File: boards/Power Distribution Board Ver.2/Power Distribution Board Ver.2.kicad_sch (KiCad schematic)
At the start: 89 parts, among them J1 Screw_Terminal_01x02, J2 Screw_Terminal_01x06, J3 Screw_Terminal_01x06, J4 Screw_Terminal_01x06, K1 Relay, K2 Relay, K3 Relay, K4 Relay, K5 Relay, K6 Relay, SW1 SW_Push_Open, U1 SIC431AED-T1-GE3, U2 SIC431AED-T1-GE3, U3 SIC431AED-T1-GE3

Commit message: Edit PCB
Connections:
- net 5V_OUT_1: no longer D7.2 (K), D9.2 (K)
- net 5V_OUT_2: now also D7.2 (K)
- net 5V_OUT_3: now also D9.2 (K)
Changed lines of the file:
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@@
     (effects (font (size 1.27 1.27)) (justify left))
   )
-  (hierarchical_label "5V_OUT_1" (shape output) (at 229.87 226.06 0) (fields_autoplaced)
+  (hierarchical_label "5V_OUT_2" (shape output) (at 229.87 226.06 0) (fields_autoplaced)
     (effects (font (size 1.27 1.27)) (justify left))
   )
@@
     (effects (font (size 1.27 1.27)) (justify left))
   )
-  (hierarchical_label "5V_OUT_1" (shape output) (at 226.822 286.512 0) (fields_autoplaced)
+  (hierarchical_label "5V_OUT_3" (shape output) (at 226.822 286.512 0) (fields_autoplaced)
     (effects (font (size 1.27 1.27)) (justify left))
   )

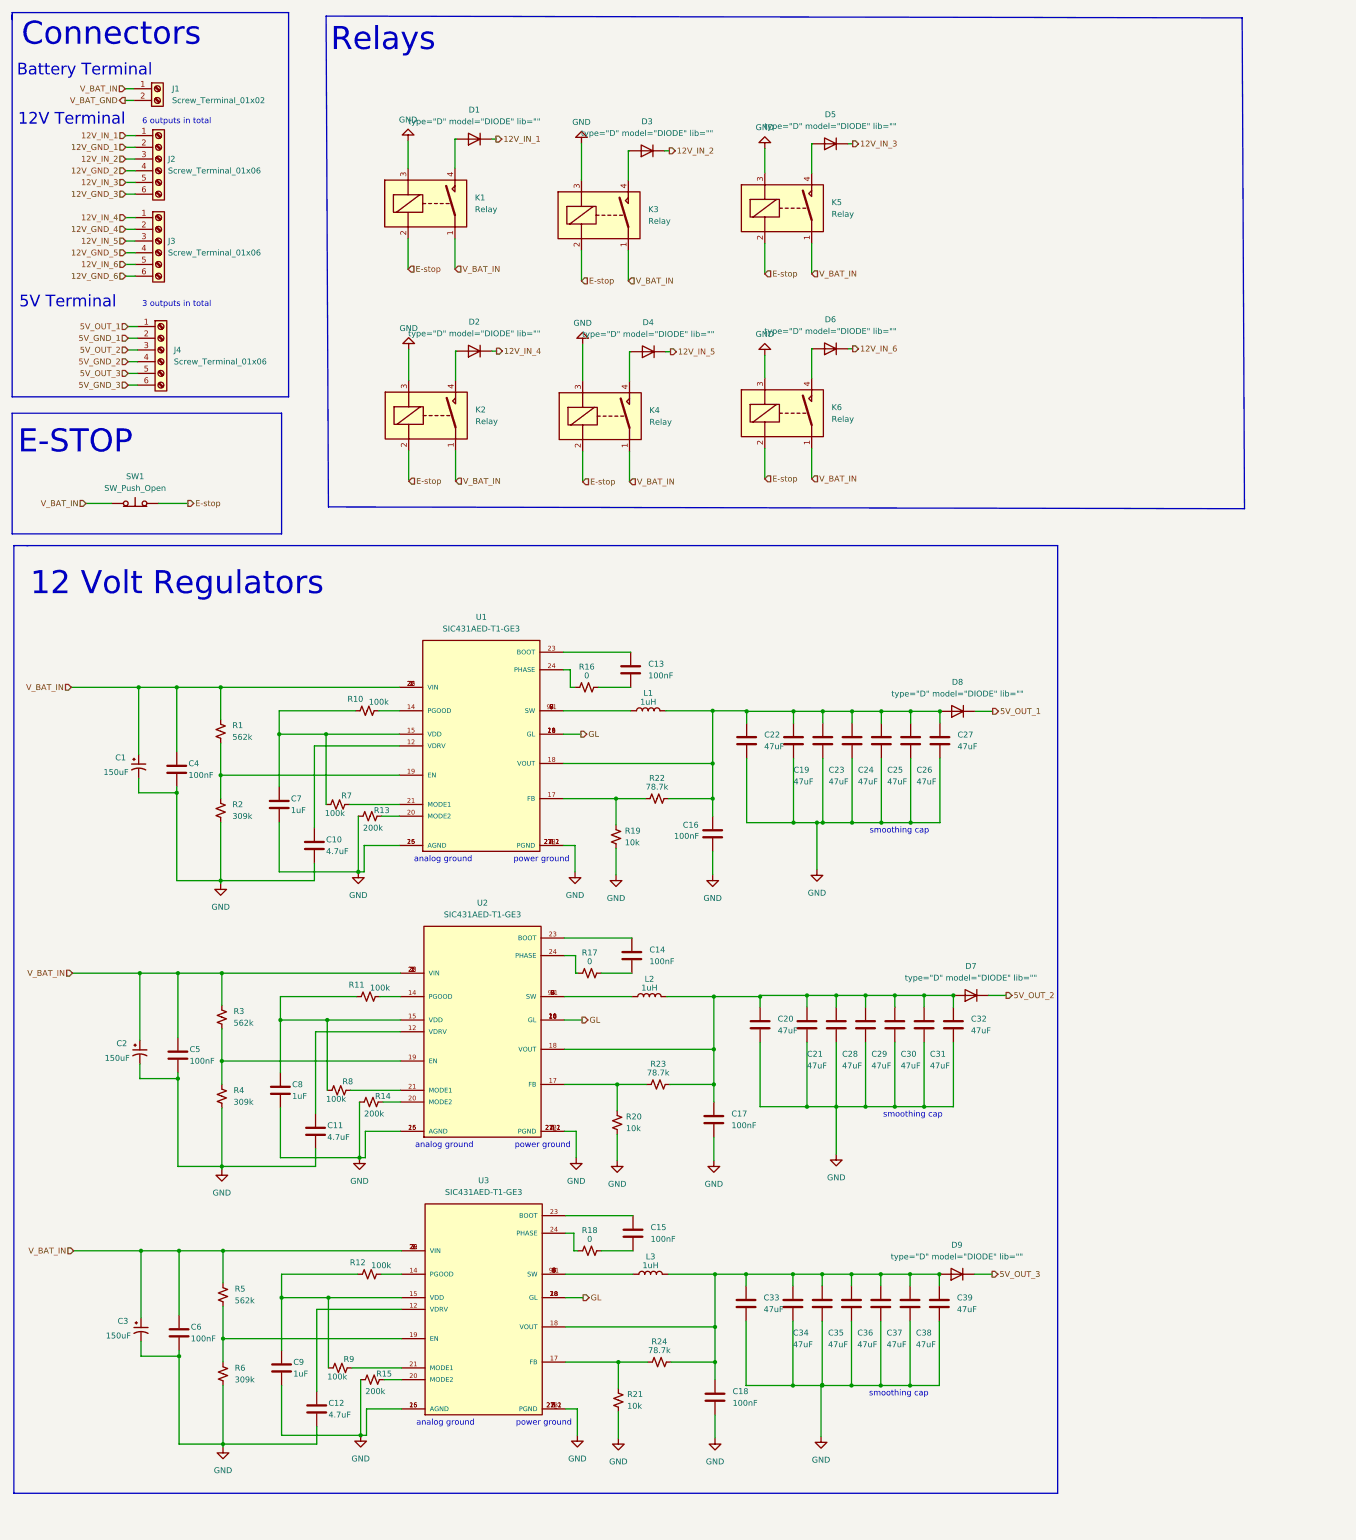
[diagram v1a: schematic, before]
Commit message: Updated GND
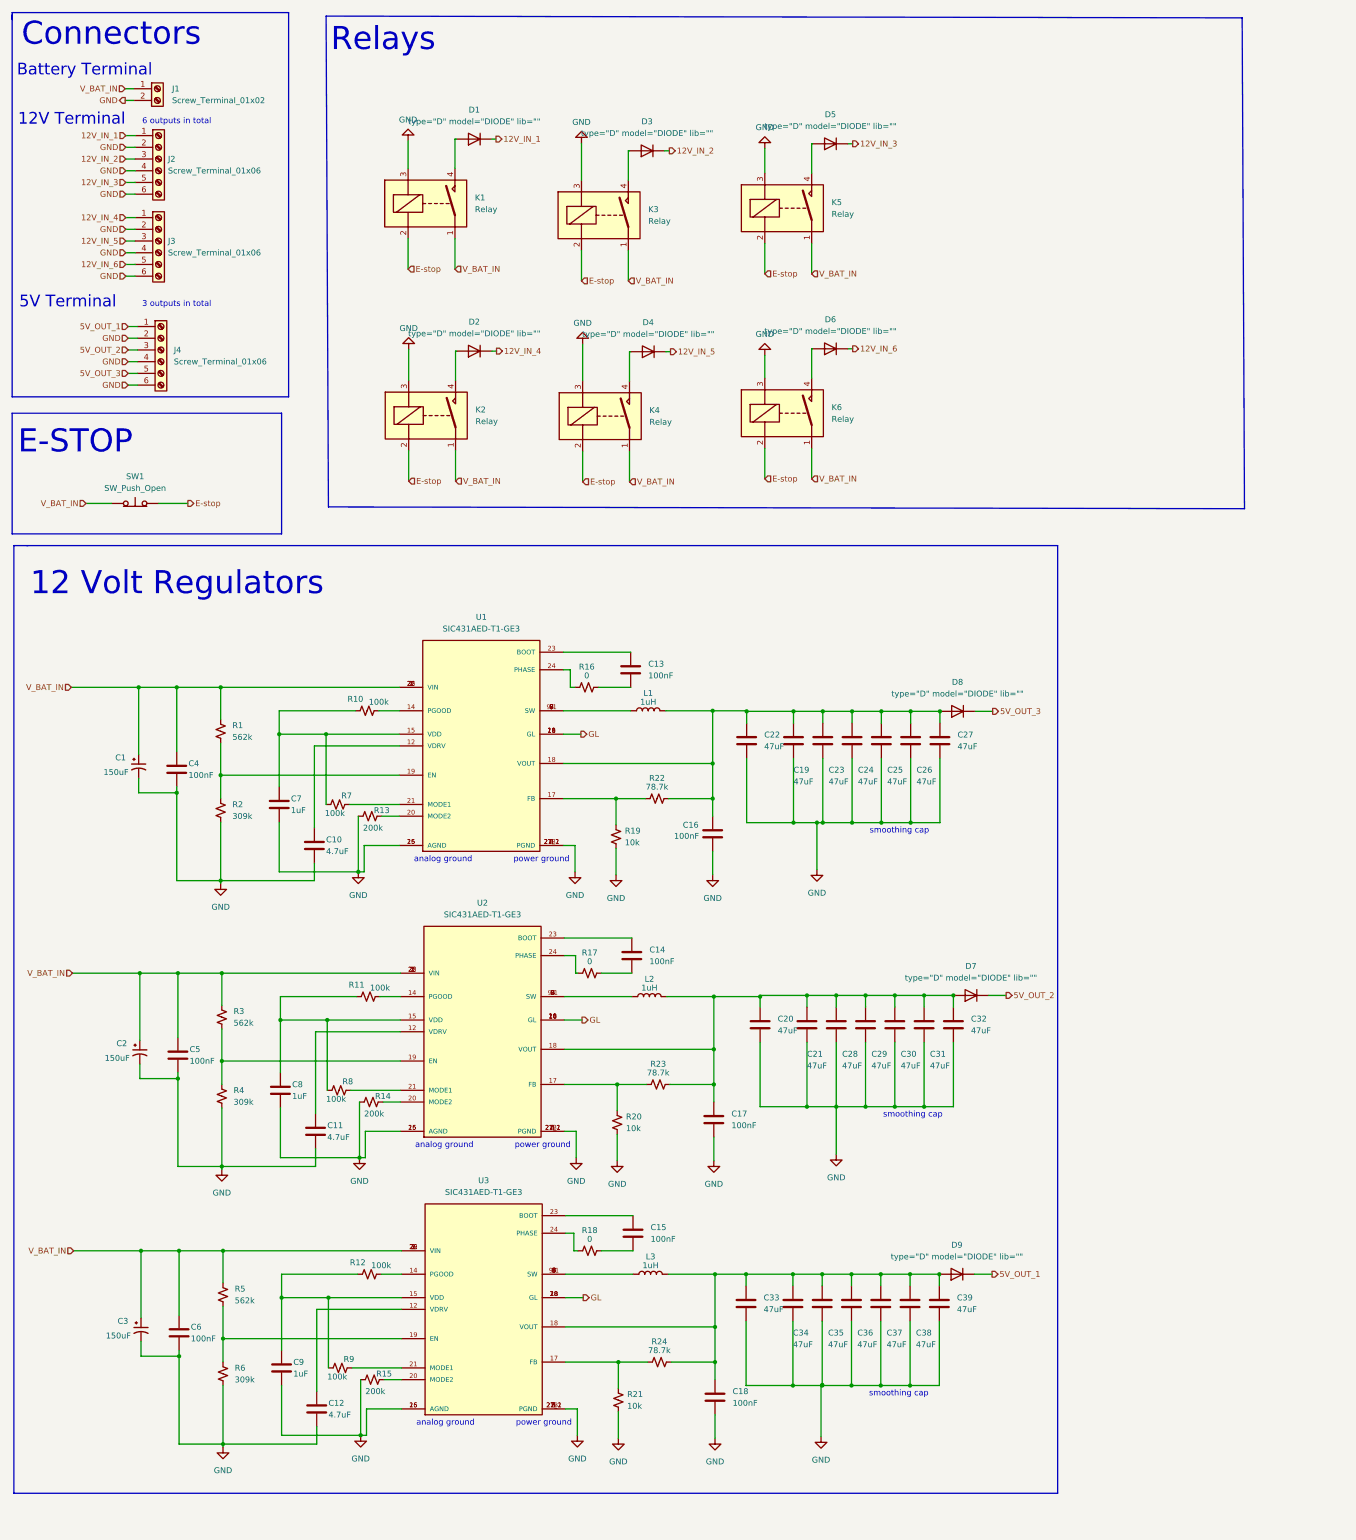
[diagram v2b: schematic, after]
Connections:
- net 12V_GND_1 is gone; now on net GND: J2.2 (Pin_2)
- net 12V_GND_2 is gone; now on net GND: J2.4 (Pin_4)
- net 12V_GND_3 is gone; now on net GND: J2.6 (Pin_6)
- net 12V_GND_4 is gone; now on net GND: J3.2 (Pin_2)
- net 12V_GND_5 is gone; now on net GND: J3.4 (Pin_4)
- net 12V_GND_6 is gone; now on net GND: J3.6 (Pin_6)
- net 5V_GND_1 is gone; now on net GND: J4.2 (Pin_2)
- net 5V_GND_2 is gone; now on net GND: J4.4 (Pin_4)
- net 5V_GND_3 is gone; now on net GND: J4.6 (Pin_6)
- net V_BAT_GND is gone; now on net GND: J1.2 (Pin_2)
- net 5V_OUT_1: now also D9.2 (K); no longer D8.2 (K)
- net 5V_OUT_3: now also D8.2 (K); no longer D9.2 (K)
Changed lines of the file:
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@@
     (effects (font (size 1.27 1.27)) (justify left))
   )
-  (hierarchical_label "5V_GND_3" (shape input) (at 39.497 93.726 180) (fields_autoplaced)
+  (hierarchical_label "GND" (shape input) (at 39.497 93.726 180) (fields_autoplaced)
     (effects (font (size 1.27 1.27)) (justify right))
   )
@@
     (effects (font (size 1.27 1.27)) (justify right))
   )
-  (hierarchical_label "12V_GND_3" (shape input) (at 38.989 52.324 180) (fields_autoplaced)
+  (hierarchical_label "GND" (shape input) (at 38.989 52.324 180) (fields_autoplaced)
     (effects (font (size 1.27 1.27)) (justify right))
   )
@@
     (effects (font (size 1.27 1.27)) (justify left))
   )
-  (hierarchical_label "12V_GND_1" (shape input) (at 38.989 42.164 180) (fields_autoplaced)
+  (hierarchical_label "GND" (shape input) (at 38.989 42.164 180) (fields_autoplaced)
     (effects (font (size 1.27 1.27)) (justify right))
   )
-  (hierarchical_label "5V_GND_2" (shape input) (at 39.497 88.646 180) (fields_autoplaced)
+  (hierarchical_label "GND" (shape input) (at 39.497 88.646 180) (fields_autoplaced)
     (effects (font (size 1.27 1.27)) (justify right))
   )
@@
     (effects (font (size 1.27 1.27)) (justify left))
   )
-  (hierarchical_label "12V_GND_5" (shape input) (at 38.989 65.024 180) (fields_autoplaced)
+  (hierarchical_label "GND" (shape input) (at 38.989 65.024 180) (fields_autoplaced)
     (effects (font (size 1.27 1.27)) (justify right))
   )
@@
     (effects (font (size 1.27 1.27)) (justify left))
   )
-  (hierarchical_label "12V_GND_2" (shape input) (at 38.989 47.244 180) (fields_autoplaced)
+  (hierarchical_label "GND" (shape input) (at 38.989 47.244 180) (fields_autoplaced)
     (effects (font (size 1.27 1.27)) (justify right))
   )
@@
     (effects (font (size 1.27 1.27)) (justify left))
   )
-  (hierarchical_label "V_BAT_GND" (shape output) (at 38.862 32.004 180) (fields_autoplaced)
+  (hierarchical_label "GND" (shape output) (at 38.862 32.004 180) (fields_autoplaced)
     (effects (font (size 1.27 1.27)) (justify right))
   )
@@
     (effects (font (size 1.27 1.27)) (justify left))
   )
-  (hierarchical_label "5V_OUT_3" (shape output) (at 226.822 286.512 0) (fields_autoplaced)
+  (hierarchical_label "5V_OUT_1" (shape output) (at 226.822 286.512 0) (fields_autoplaced)
     (effects (font (size 1.27 1.27)) (justify left))
   )
-  (hierarchical_label "5V_OUT_1" (shape output) (at 226.949 164.465 0) (fields_autoplaced)
+  (hierarchical_label "5V_OUT_3" (shape output) (at 226.949 164.465 0) (fields_autoplaced)
     (effects (font (size 1.27 1.27)) (justify left))
   )
@@
     (effects (font (size 1.27 1.27)) (justify left))
   )
-  (hierarchical_label "5V_GND_1" (shape input) (at 39.497 83.566 180) (fields_autoplaced)
+  (hierarchical_label "GND" (shape input) (at 39.497 83.566 180) (fields_autoplaced)
     (effects (font (size 1.27 1.27)) (justify right))
   )
@@
     (effects (font (size 1.27 1.27)) (justify left))
   )
-  (hierarchical_label "12V_GND_4" (shape input) (at 38.989 59.944 180) (fields_autoplaced)
+  (hierarchical_label "GND" (shape input) (at 38.989 59.944 180) (fields_autoplaced)
     (effects (font (size 1.27 1.27)) (justify right))
   )
-  (hierarchical_label "12V_GND_6" (shape input) (at 38.989 70.104 180) (fields_autoplaced)
+  (hierarchical_label "GND" (shape input) (at 38.989 70.104 180) (fields_autoplaced)
     (effects (font (size 1.27 1.27)) (justify right))
   )

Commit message: PCBPCB Circuit Design Finished
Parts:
- renumbered C20 to C19, C21 to C20, C28 to C21, C29 to C22, C30 to C23, C31 to C24, C32 to C25, C22 to C26, C19 to C27, C23 to C28, C24 to C29, C25 to C30, C26 to C31, C27 to C32

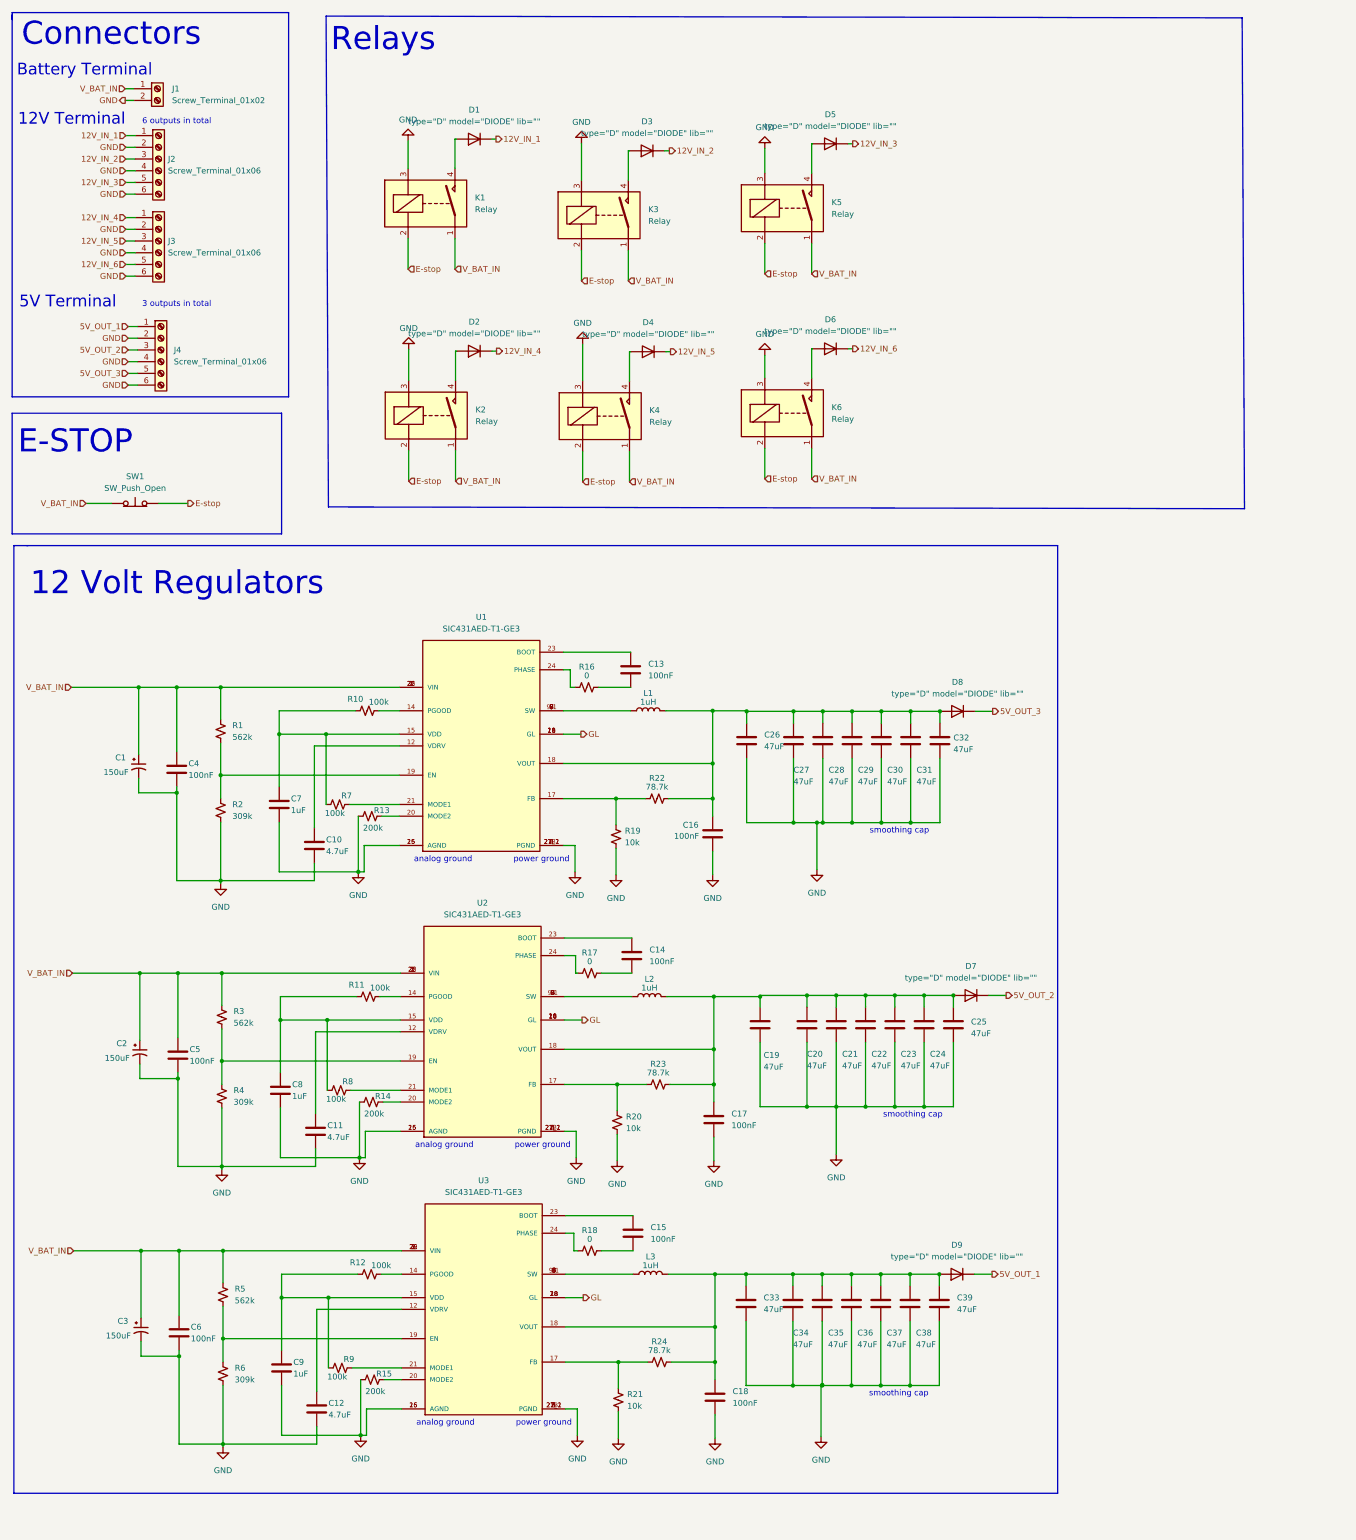
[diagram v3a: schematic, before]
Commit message: Added USB port
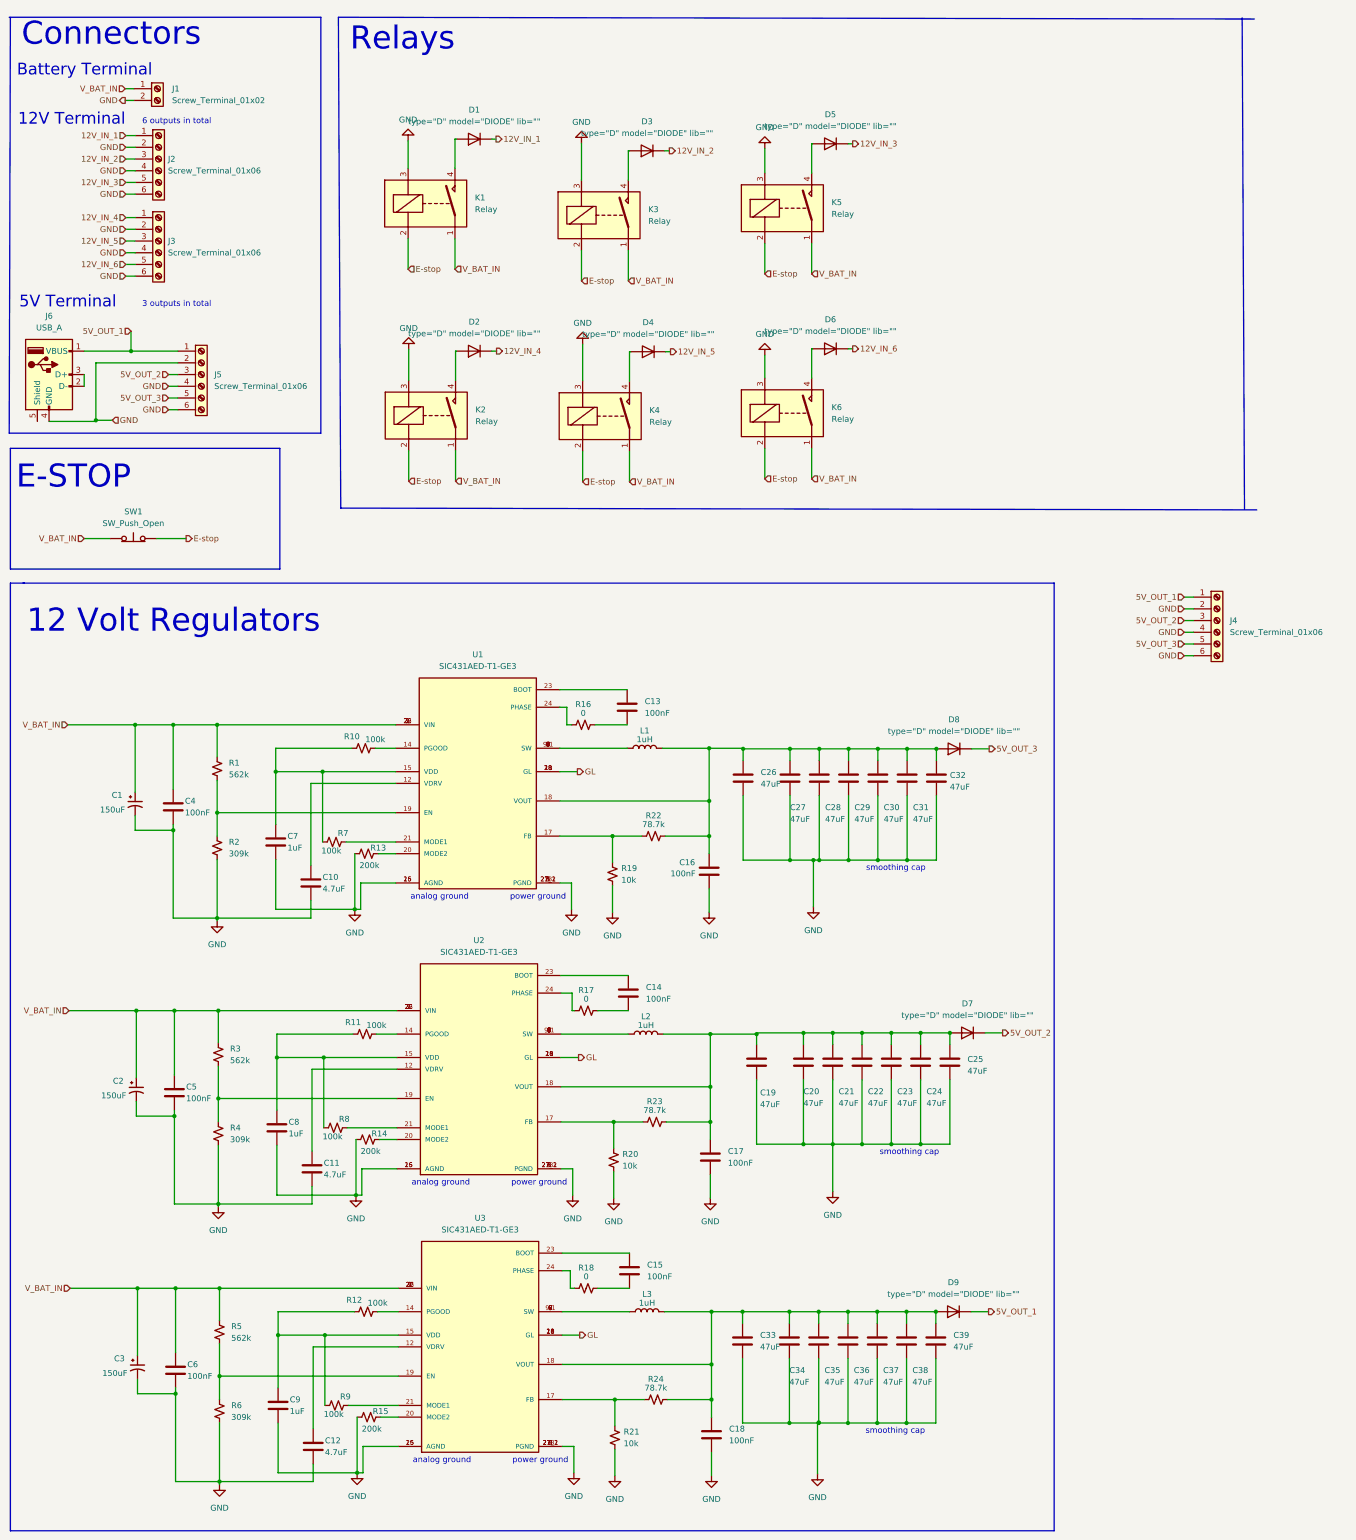
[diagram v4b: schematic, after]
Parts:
- added J5: Screw_Terminal_01x06, power_board_support:691137710006, symbol Connector:Screw_Terminal_01x06
- added J6: USB_A, Connector_USB:USB_A_CNCTech_1001-011-01101_Horizontal, symbol Connector:USB_A
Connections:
- net 5V_OUT_1: now also J5.1 (Pin_1), J6.1 (VBUS)
- net 5V_OUT_2: now also J5.3 (Pin_3)
- net 5V_OUT_3: now also J5.5 (Pin_5)
- net GND: now also J5.2 (Pin_2), J5.4 (Pin_4), J5.6 (Pin_6), J6.4 (GND)
- new net: J6.2 (D-), J6.3 (D+)
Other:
- moved on the sheet: C1, C10, C11, C12, C13, C14, C15, C16, C17, C18, C19, C2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
